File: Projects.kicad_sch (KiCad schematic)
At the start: 16 parts, among them P1 7-215079-4, P2 7-215079-4, SW1 SW_Push, SW2 SW_Push, SW3 SW_Push, U1 MAX30102, U2 SSD1306

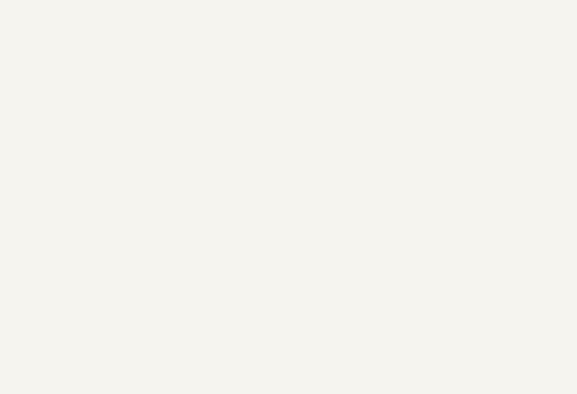
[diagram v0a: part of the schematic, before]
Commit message: feat: Se agrega conector JST 1X3
Se agrega conector para la alimentación del circuito
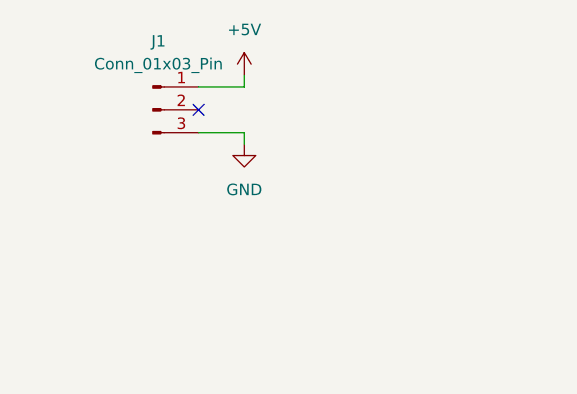
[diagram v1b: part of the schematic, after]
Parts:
- added J1: Conn_01x03_Pin, Connector_JST:JST_EH_B3B-EH-A_1x03_P2.50mm_Vertical, symbol Connector:Conn_01x03_Pin
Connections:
- net +5V: now also J1.1 (Pin_1)
- net GND: now also J1.3 (Pin_3)
- no-connect marks 21 -> 22
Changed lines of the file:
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@@
+	)
+	(no_connect
+		(at 39.37 40.64)
 	)
 	(no_connect
@@
 	(wire
 		(pts
+			(xy 44.45 38.1) (xy 39.37 38.1)
+		)
+		(stroke
+			(width 0)
+			(type default)
+		)
+	)
+	(wire
+		(pts
 			(xy 21.59 135.89) (xy 33.02 135.89)
 		)
@@
 	(wire
 		(pts
+			(xy 44.45 43.18) (xy 39.37 43.18)
+		)
+		(stroke
+			(width 0)
+			(type default)
+		)
+	)
+	(wire
+		(pts
 			(xy 165.1 69.85) (xy 171.45 69.85)
 		)
@@
 	(wire
 		(pts
+			(xy 44.45 44.45) (xy 44.45 43.18)
+		)
+		(stroke
+			(width 0)
+			(type default)
+		)
+	)
+	(wire
+		(pts
 			(xy 33.02 109.22) (xy 33.02 113.03)
 		)
@@
 		(pts
 			(xy 237.49 91.44) (xy 241.3 91.44)
+		)
+		(stroke
+			(width 0)
+			(type default)
+		)
+	)
+	(wire
+		(pts
+			(xy 44.45 36.83) (xy 44.45 38.1)
 		)
 		(stroke
@@
 	)
 	(symbol
+		(lib_id "power:+5V")
+		(at 44.45 36.83 0)
+		(unit 1)
+		(exclude_from_sim no)
+		(in_bom yes)
+		(on_board yes)
+		(dnp no)
+		(fields_autoplaced yes)
+		(property "Reference" "#PWR018"
+			(at 44.45 40.64 0)
+			(effects
+				(font
+					(size 1.27 1.27)
+				)
+				(hide yes)
+			)
+		)
+		(property "Value" "+5V"
+			(at 44.45 31.75 0)
+			(effects
+				(font
+					(size 1.27 1.27)
+				)
+			)
+		)
+		(property "Footprint" ""
+			(at 44.45 36.83 0)
+			(effects
+				(font
+					(size 1.27 1.27)
+				)
+				(hide yes)
+			)
+		)
+		(property "Datasheet" ""
+			(at 44.45 36.83 0)
+			(effects
+				(font
+					(size 1.27 1.27)
+				)
+				(hide yes)
+			)
+		)
+		(property "Description" "Power symbol creates a global label with name \"+5V\""
+			(at 44.45 36.83 0)
+			(effects
+				(font
+					(size 1.27 1.27)
+				)
+				(hide yes)
+			)
+		)
+		(pin "1"
+		)
+		(instances
+			(project ""
+				(path "/067f39fb-7e47-4284-ac21-d536d7af9487"
+					(reference "#PWR018")
+					(unit 1)
+				)
+			)
+		)
+	)
+	(symbol
 		(lib_id "Switch:SW_Push")
 		(at 33.02 129.54 90)
@@
 	)
 	(symbol
+		(lib_id "power:GND")
+		(at 44.45 44.45 0)
+		(unit 1)
+		(exclude_from_sim no)
+		(in_bom yes)
+		(on_board yes)
+		(dnp no)
+		(fields_autoplaced yes)
+		(property "Reference" "#PWR019"
+			(at 44.45 50.8 0)
+			(effects
+				(font
+					(size 1.27 1.27)
+				)
+				(hide yes)
+			)
+		)
+		(property "Value" "GND"
+			(at 44.45 49.53 0)
+			(effects
+				(font
+					(size 1.27 1.27)
+				)
+			)
+		)
+		(property "Footprint" ""
+			(at 44.45 44.45 0)
+			(effects
+				(font
+					(size 1.27 1.27)
+				)
+				(hide yes)
+			)
+		)
+		(property "Datasheet" ""
+			(at 44.45 44.45 0)
+			(effects
+				(font
+					(size 1.27 1.27)
+				)
+				(hide yes)
+			)
+		)
+		(property "Description" "Power symbol creates a global label with name \"GND\" , ground"
+			(at 44.45 44.45 0)
+			(effects
+				(font
+					(size 1.27 1.27)
+				)
+				(hide yes)
+			)
+		)
+		(pin "1"
+		)
+		(instances
+			(project ""
+				(path "/067f39fb-7e47-4284-ac21-d536d7af9487"
+					(reference "#PWR019")
+					(unit 1)
+				)
+			)
+		)
+	)
+	(symbol
 		(lib_id "power:+5V")
 		(at 142.24 62.23 0)
@@
 					(unit 1)
 				)
+			)
+		)
+	)
+	(symbol
+		(lib_id "Connector:Conn_01x03_Pin")
+		(at 34.29 40.64 0)
+		(unit 1)
+		(exclude_from_sim no)
+		(in_bom yes)
+		(on_board yes)
+		(dnp no)
+		(fields_autoplaced yes)
+		(property "Reference" "J1"
+			(at 34.925 33.02 0)
+			(effects
+				(font
+					(size 1.27 1.27)
+				)
+			)
+		)
+		(property "Value" "Conn_01x03_Pin"
+			(at 34.925 35.56 0)
+			(effects
+				(font
+					(size 1.27 1.27)
+				)
+			)
+		)
+		(property "Footprint" "Connector_JST:JST_EH_B3B-EH-A_1x03_P2.50mm_Vertical"
+			(at 34.29 40.64 0)
+			(effects
+				(font
+					(size 1.27 1.27)
+				)
+				(hide yes)
+			)
+		)
+		(property "Datasheet" "~"
+			(at 34.29 40.64 0)
+			(effects
+				(font
+					(size 1.27 1.27)
+				)
+				(hide yes)
+			)
+		)
+		(property "Description" "Generic connector, single row, 01x03, script generated"
+			(at 34.29 40.64 0)
+			(effects
+				(font
+					(size 1.27 1.27)
+				)
+				(hide yes)
+			)
+		)
+		(pin "2"
+		)
+		(pin "1"
+		)
+		(pin "3"
+		)
+		(instances
+			(project ""
+				(path "/067f39fb-7e47-4284-ac21-d536d7af9487"
+					(reference "J1")
+					(unit 1)
+				)
